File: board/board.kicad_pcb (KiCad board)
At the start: 2 copper layers, 50.8 x 22.9 mm, 10 parts, among them J1 MOTION DETECTOR, J2 EXT BUTTON, U1 APA102 (RGB), U2 APA102 (W)

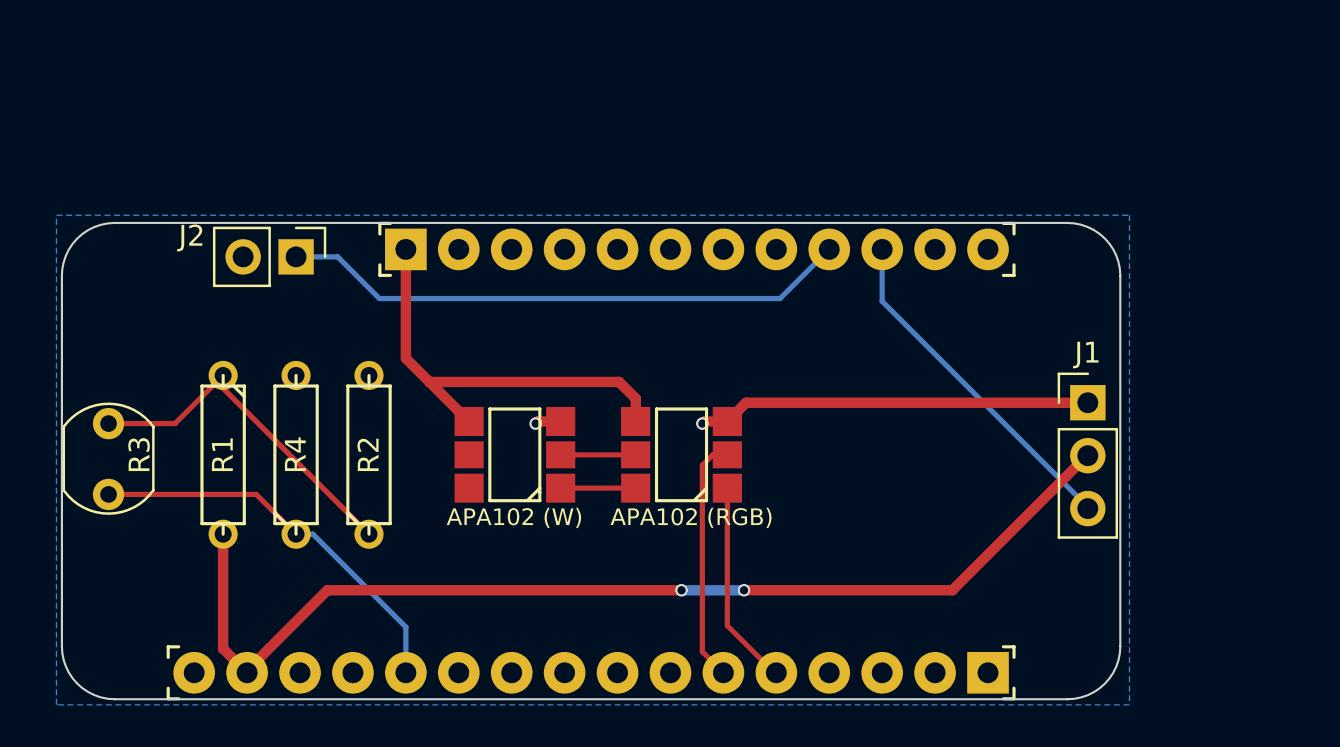
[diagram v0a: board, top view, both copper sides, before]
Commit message: Add attiny85 to control power
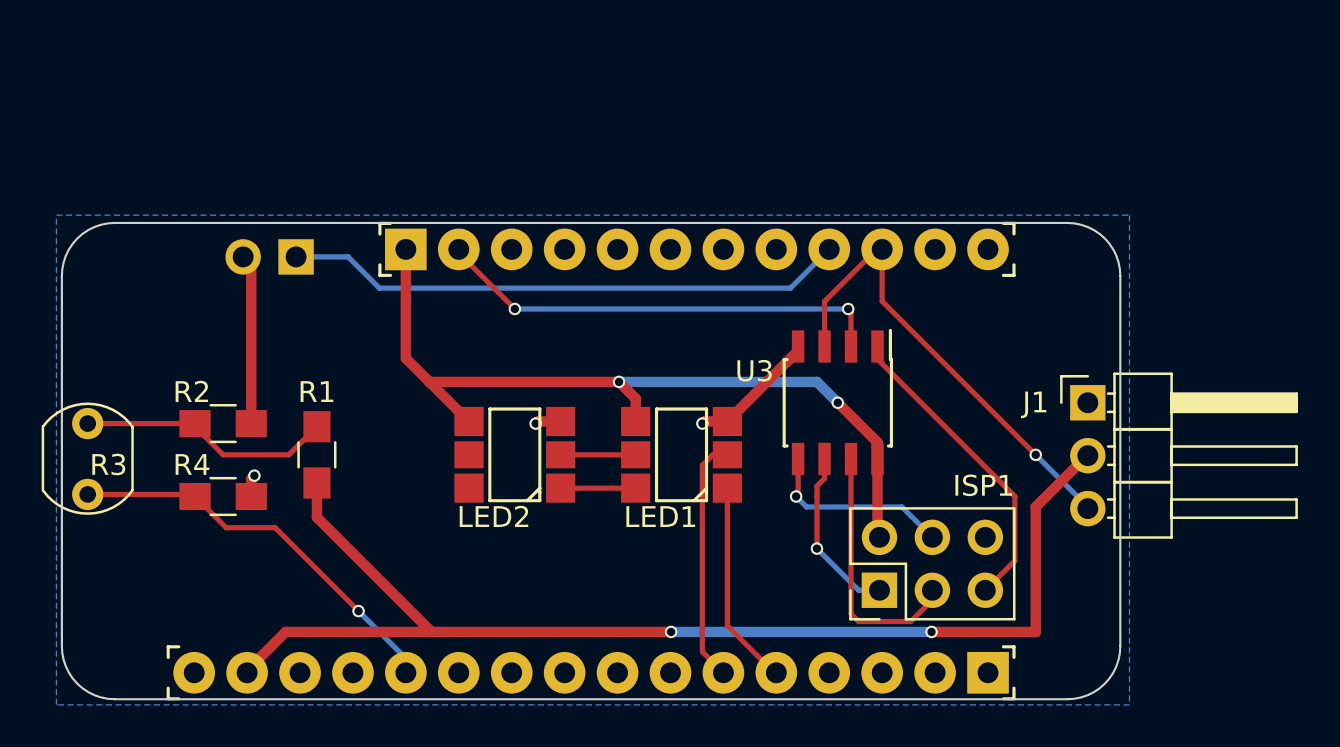
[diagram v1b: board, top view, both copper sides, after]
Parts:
- added ISP1: AVR-ISP-6, Pin_Headers:Pin_Header_Straight_2x03_Pitch2.54mm, F.Cu at (151.0, 120.5)
- added U3: ATTINY85-20PU, Housings_SOIC:SOIC-8_3.9x4.9mm_Pitch1.27mm, F.Cu at (149.0, 111.5)
- J1: footprint Pin_Headers:Pin_Header_Straight_1x03_Pitch2.54mm -> Pin_Headers:Pin_Header_Angled_1x03_Pitch2.54mm
- J2: footprint Pin_Headers:Pin_Header_Straight_1x02_Pitch2.54mm -> Pin_Headers:Pin_Header_Angled_1x02_Pitch2.54mm; moved to B.Cu
- R1, R2, R4: footprint Discret:R3 -> Resistors_SMD:R_0805_HandSoldering
- moved R2 7.16 mm to (119.5, 112.5), turned to 0 degrees
- moved R1 4.50 mm to (124.0, 114.0)
- moved R4 4.03 mm to (119.5, 116.0), turned to 0 degrees
- moved R3 1.00 mm to (113.0, 112.5)
- turned J2 to 90 degrees
- renumbered U1 to LED1, U2 to LED2
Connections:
- JP3 pad 2: (no net) -> /EN
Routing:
- net /EN: track 0.00 -> 23.3 mm, vias 0 -> 2
- net /VBAT: track 21.3 -> 39.9 mm, vias 0 -> 2
- net Net-(ISP1-Pad5): track 0.00 -> 15.1 mm
- net Net-(ISP1-Pad3): track 0.00 -> 12.4 mm
- net Net-(ISP1-Pad4): track 0.00 -> 9.19 mm, vias 0 -> 1
- net Net-(ISP1-Pad1): track 0.00 -> 8.28 mm, vias 0 -> 1
- net /D5: track 16.5 -> 22.5 mm, vias 0 -> 1
- net VCC: track 51.9 -> 57.8 mm
- net Net-(R1-Pad1): track 17.2 -> 12.4 mm
- net GND: track 20.2 -> 16.7 mm, vias 2 -> 3
- net /A0: track 19.4 -> 19.2 mm, vias 0 -> 1

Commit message: Add protection resistors
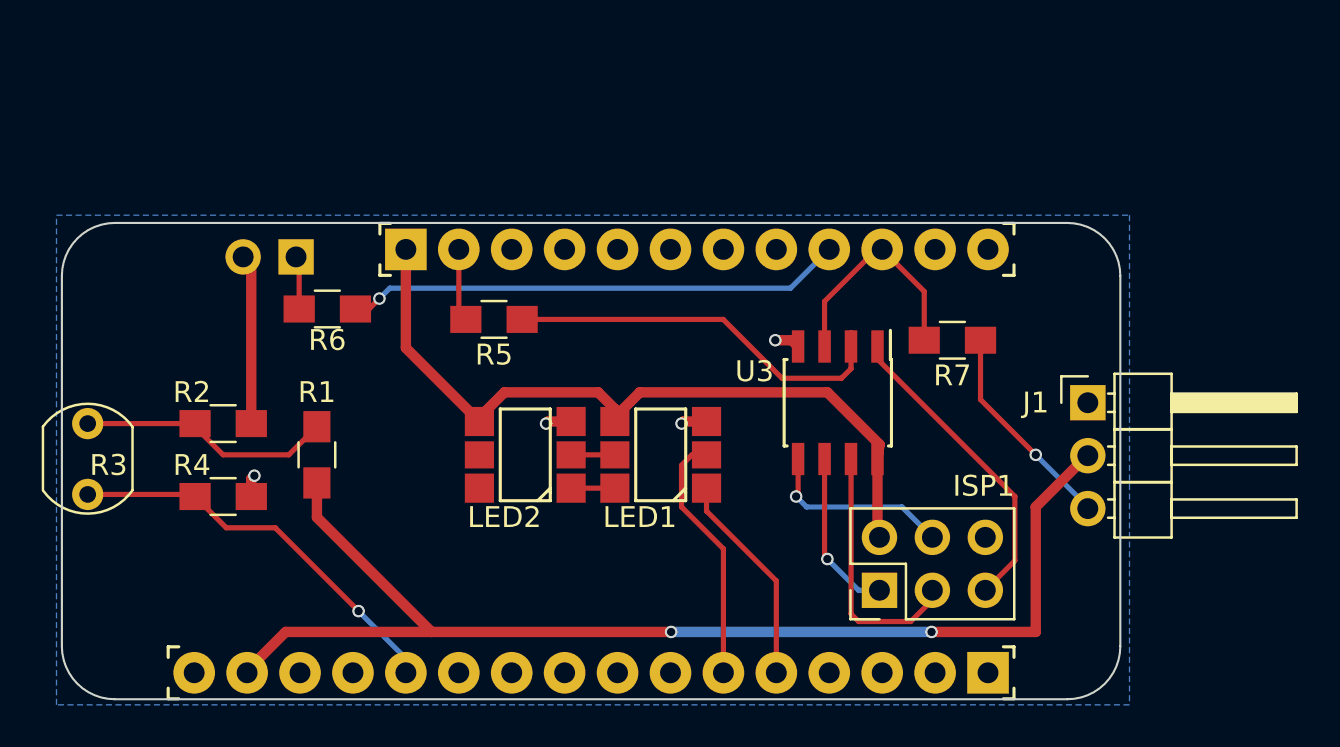
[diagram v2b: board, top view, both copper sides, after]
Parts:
- added R5: 1K, Resistors_SMD:R_0805_HandSoldering, F.Cu at (132.5, 107.5)
- added R6: 1K, Resistors_SMD:R_0805_HandSoldering, F.Cu at (124.5, 107.0)
- added R7: 1K, Resistors_SMD:R_0805_HandSoldering, F.Cu at (154.5, 108.5)
- moved LED1 1.00 mm to (140.5, 114.0)
- moved LED2 0.50 mm to (134.0, 114.0)
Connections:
- J1 pad 3: /D5 -> Net-(J1-Pad3)
- J2 pad 1: /D6 -> Net-(J2-Pad1)
- U3 pad 2: /EN -> Net-(R5-Pad1)
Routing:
- net Net-(R5-Pad1): track 0.00 -> 19.5 mm
- net /EN: track 23.3 -> 3.84 mm, vias 2 -> 0
- net /D5: track 22.5 -> 11.2 mm, vias 1 -> 0
- net Net-(J1-Pad3): track 0.00 -> 10.3 mm, vias 0 -> 1
- net GND: track 16.7 -> 13.1 mm, vias 3 -> 4
- net /D6: track 27.0 -> 23.9 mm, vias 0 -> 1
- net Net-(J2-Pad1): track 0.00 -> 2.56 mm
- net /VBAT: track 39.9 -> 38.0 mm, vias 2 -> 0
- net Net-(LED1-Pad6): track 3.60 -> 2.10 mm
- net Net-(LED1-Pad5): track 3.60 -> 2.10 mm

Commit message: Rework
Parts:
- moved R5 18.7 mm to (119.5, 121.0)
- moved R1 6.54 mm to (119.5, 109.2), turned to 0 degrees
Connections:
- ISP1 pad 2: /VBAT -> VCC
- JP1 pad 16: (no net) -> /~RESET
- JP3 pad 2: /EN -> (no net)
- R5 pad 2: /EN -> /~RESET
- U3 pad 8: /VBAT -> VCC
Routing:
- net VCC: track 57.8 -> 1.67 mm, vias 2 -> 0
- net /VBAT: track 38.0 -> 18.1 mm
- net Net-(R5-Pad1): track 19.5 -> 35.7 mm, vias 0 -> 2
- net GND: track 13.1 -> 9.23 mm
- net /EN: track 3.84 -> 0.00 mm
- net Net-(R1-Pad1): track 12.4 -> 8.70 mm
- net /~RESET: track 0.00 -> 3.48 mm
- net /A0: track 19.2 -> 19.8 mm
- added copper zone on F.Cu, net VCC

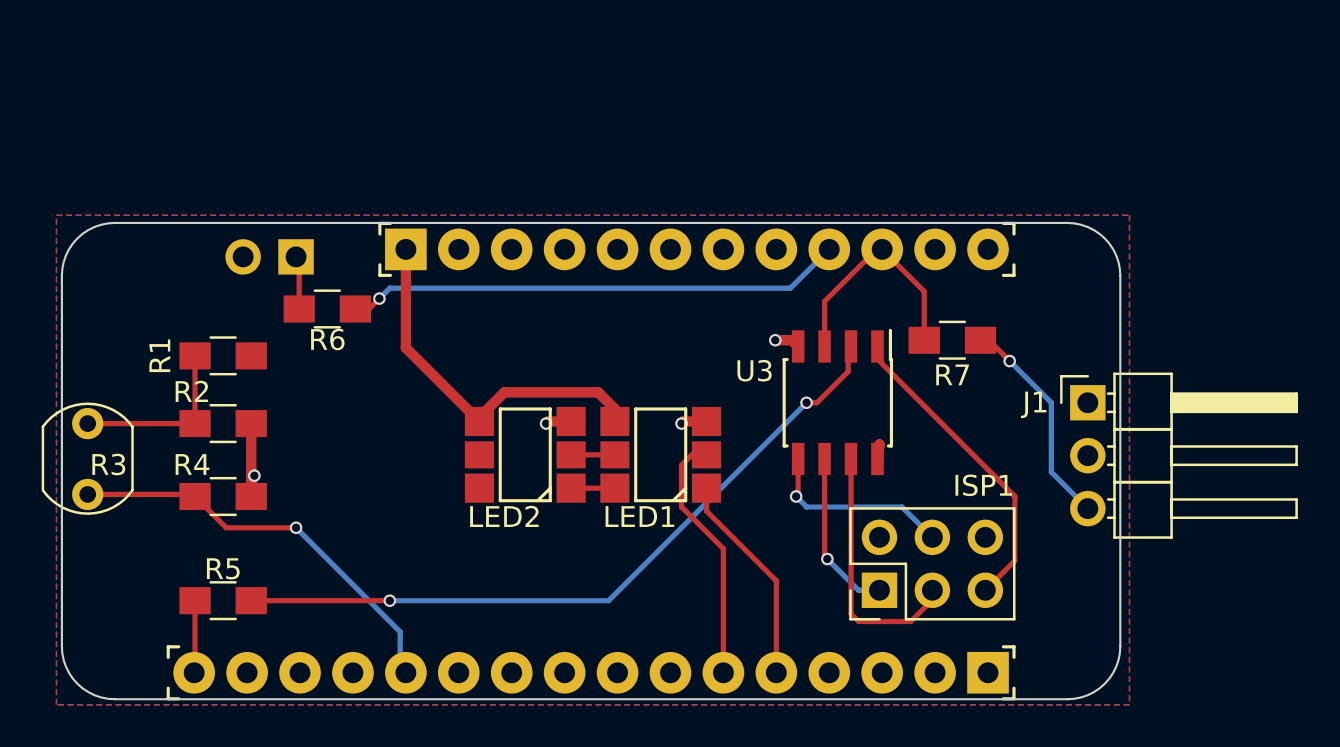
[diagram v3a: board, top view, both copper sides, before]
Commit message: Move ISP header further from LEDs to prevent shadows
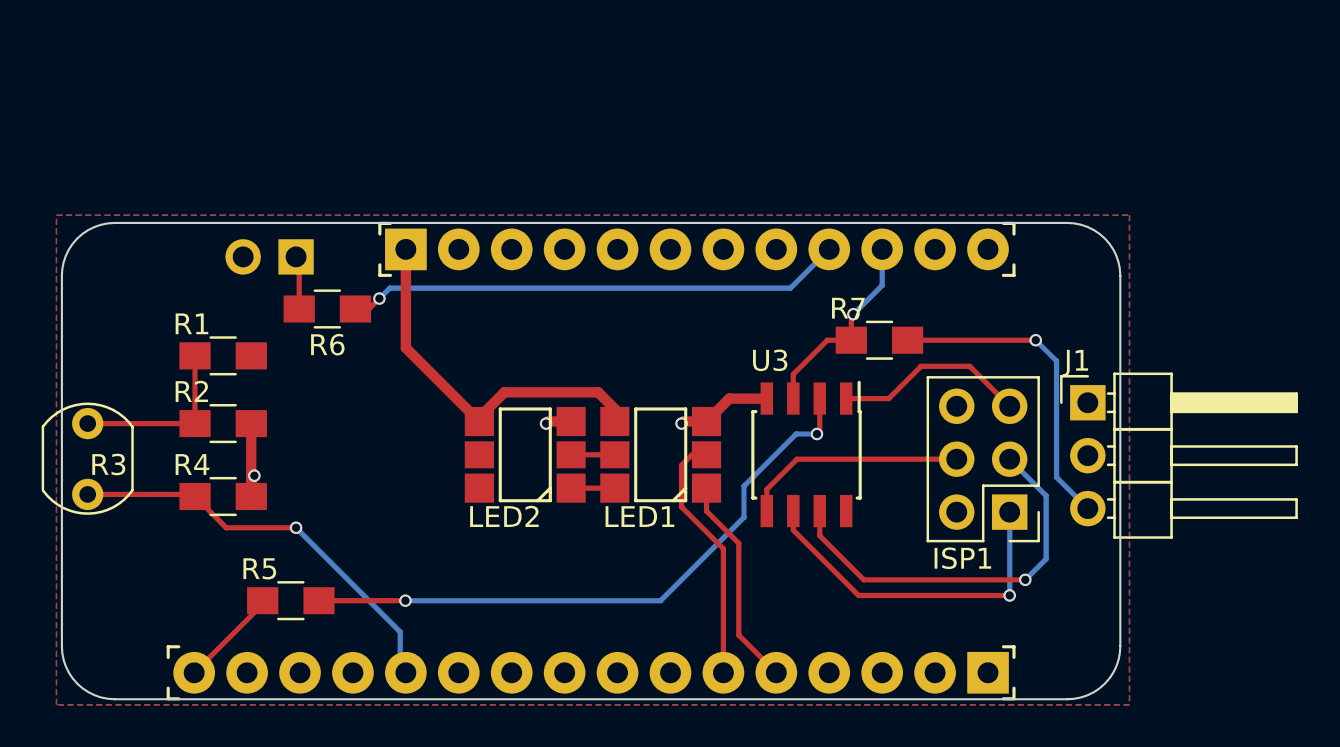
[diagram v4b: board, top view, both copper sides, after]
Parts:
- moved ISP1 7.29 mm to (157.2, 116.8), turned to 180 degrees
- moved R7 3.50 mm to (151.0, 108.5)
- moved R5 3.25 mm to (122.8, 121.0)
- moved U3 2.92 mm to (147.5, 114.0)
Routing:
- net Net-(ISP1-Pad1): track 7.98 -> 16.6 mm
- net Net-(ISP1-Pad3): track 12.4 -> 19.8 mm, vias 0 -> 1
- net Net-(R5-Pad1): track 35.7 -> 29.8 mm
- net Net-(ISP1-Pad5): track 15.1 -> 9.28 mm
- net Net-(J1-Pad3): track 10.8 -> 15.3 mm
- net GND: track 9.23 -> 11.2 mm, vias 4 -> 3
- net Net-(ISP1-Pad4): track 9.19 -> 10.8 mm, vias 1 -> 0
- net /D5: track 11.2 -> 9.63 mm, vias 0 -> 1
- net VCC: track 1.67 -> 0.15 mm
- net /~RESET: track 3.48 -> 4.88 mm

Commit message: Move headers so they'll fit inside a jar
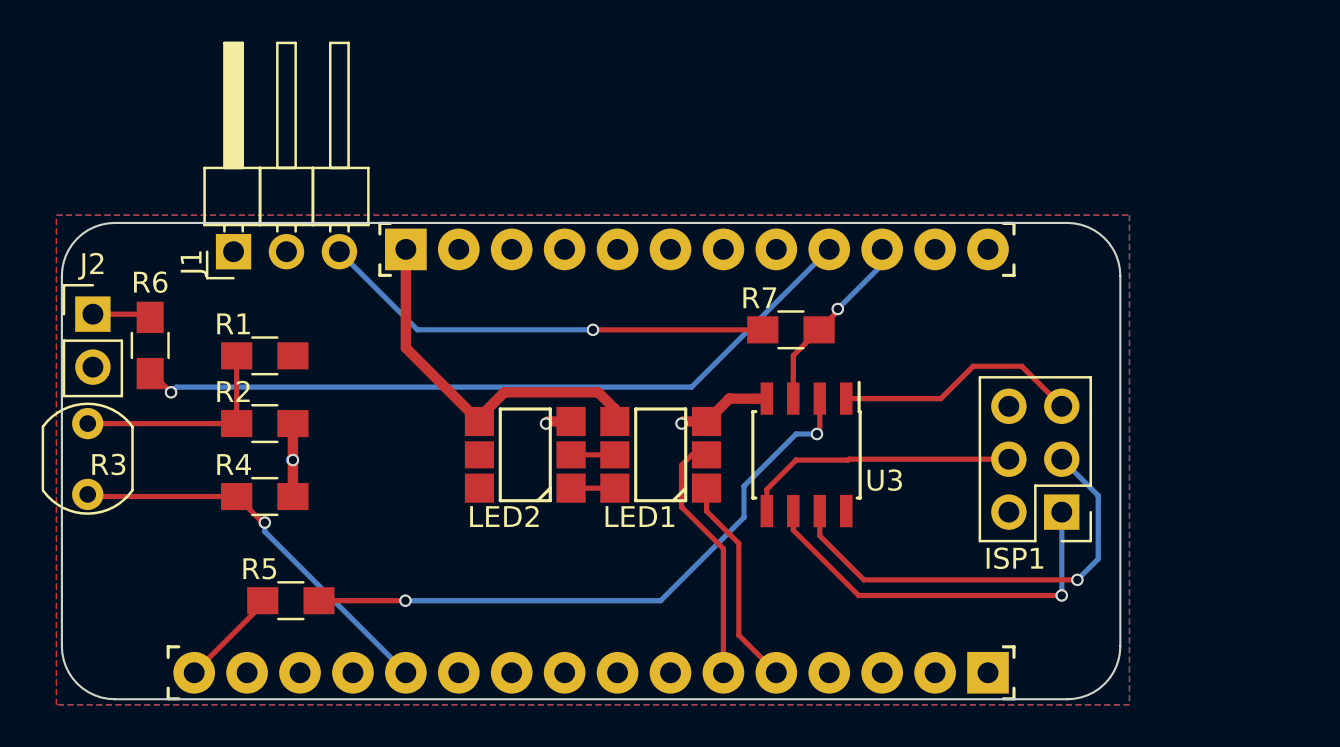
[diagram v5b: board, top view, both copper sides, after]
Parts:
- J2: footprint Pin_Headers:Pin_Header_Angled_1x02_Pitch2.54mm -> Pin_Headers:Pin_Header_Straight_1x02_Pitch2.54mm; moved to F.Cu
- moved J1 41.6 mm to (120.0, 104.2), turned to 90 degrees
- moved J2 10.1 mm to (113.2, 107.2), turned to 0 degrees
- moved R6 8.68 mm to (116.0, 108.8), turned to 270 degrees
- moved R7 4.28 mm to (146.8, 108.0), turned to 0 degrees
- moved ISP1 2.50 mm to (159.8, 116.8)
- moved R1 2.00 mm to (121.5, 109.2)
- moved R2 2.00 mm to (121.5, 112.5)
- moved R4 2.00 mm to (121.5, 116.0)
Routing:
- net /D6: track 23.9 -> 35.8 mm
- net Net-(J1-Pad3): track 15.3 -> 21.9 mm
- net Net-(ISP1-Pad5): track 9.28 -> 11.8 mm
- net Net-(ISP1-Pad4): track 10.8 -> 13.3 mm
- net Net-(ISP1-Pad1): track 16.6 -> 19.1 mm
- net Net-(ISP1-Pad3): track 19.8 -> 22.3 mm
- net GND: track 11.2 -> 9.43 mm
- net Net-(R1-Pad1): track 8.70 -> 10.4 mm
- net /D5: track 9.63 -> 8.95 mm

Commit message: Move motion detector header further inward
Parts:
- moved J1 2.50 mm to (120.0, 106.8)
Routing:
- net Net-(J1-Pad3): track 21.9 -> 20.8 mm

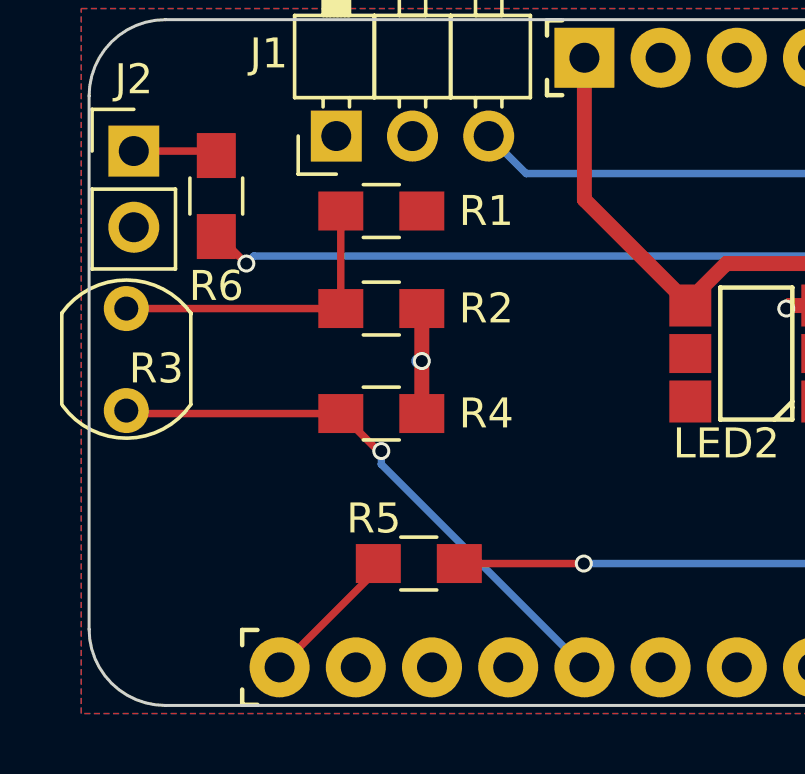
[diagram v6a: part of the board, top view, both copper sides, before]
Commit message: Fix photoresistor circuit
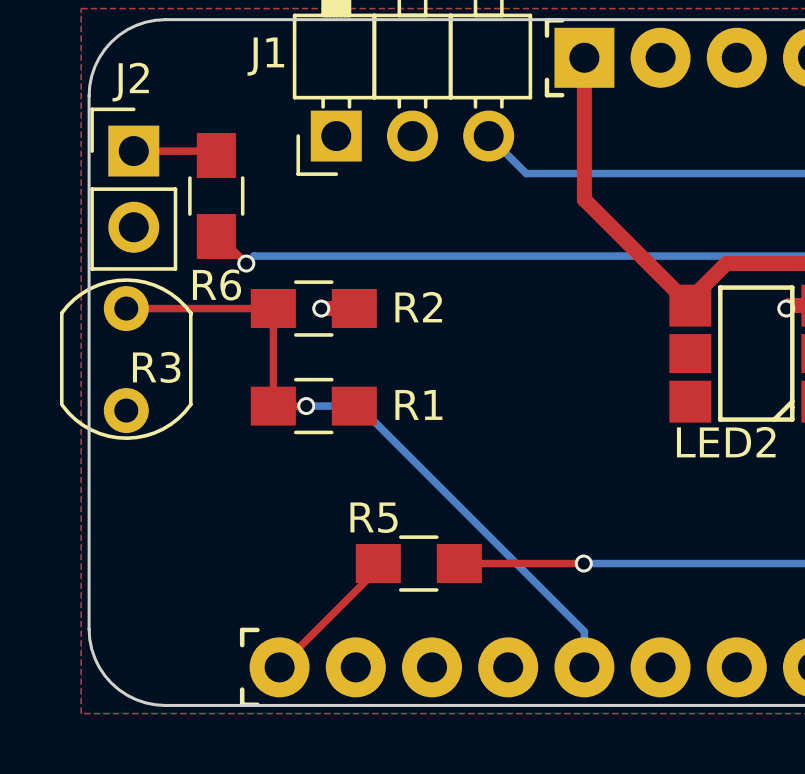
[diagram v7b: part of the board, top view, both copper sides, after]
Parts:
- removed R4: 10K, Resistors_SMD:R_0805_HandSoldering
- moved R1 6.88 mm to (119.2, 115.8)
- moved R2 2.25 mm to (119.2, 112.5)
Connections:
- R1 pad 1: Net-(R1-Pad1) -> /A0
- R2 pad 1: Net-(R1-Pad1) -> /A0
- R3 pad 1: Net-(R1-Pad1) -> /A0
- R3 pad 2: /A0 -> GND
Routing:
- net Net-(R1-Pad1): track 10.4 -> 0.00 mm
- net /A0: track 19.5 -> 24.0 mm
- net GND: track 9.43 -> 7.07 mm
